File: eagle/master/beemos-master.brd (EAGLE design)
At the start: 99.1 x 73.7 mm, 47 parts, among them CON1 BAT, CON2 JACK_DC_BARREL, CON3 SPI, IC1 32U4, IC2 MCP73831T, IC3 MCP1703CB, IC4 DMP1045U, J1 RJ123.3, J10 RJ12STRAIGHT-I2C, J2 RJ123.3, J3 RJ123.3, J4 RJ123.3, J5 RJ123.3, J6 RJ123.3, J8 RJ123.3, J9 RJ12STRAIGHT-I2C, X1 8MHz, X2 MINI-USB

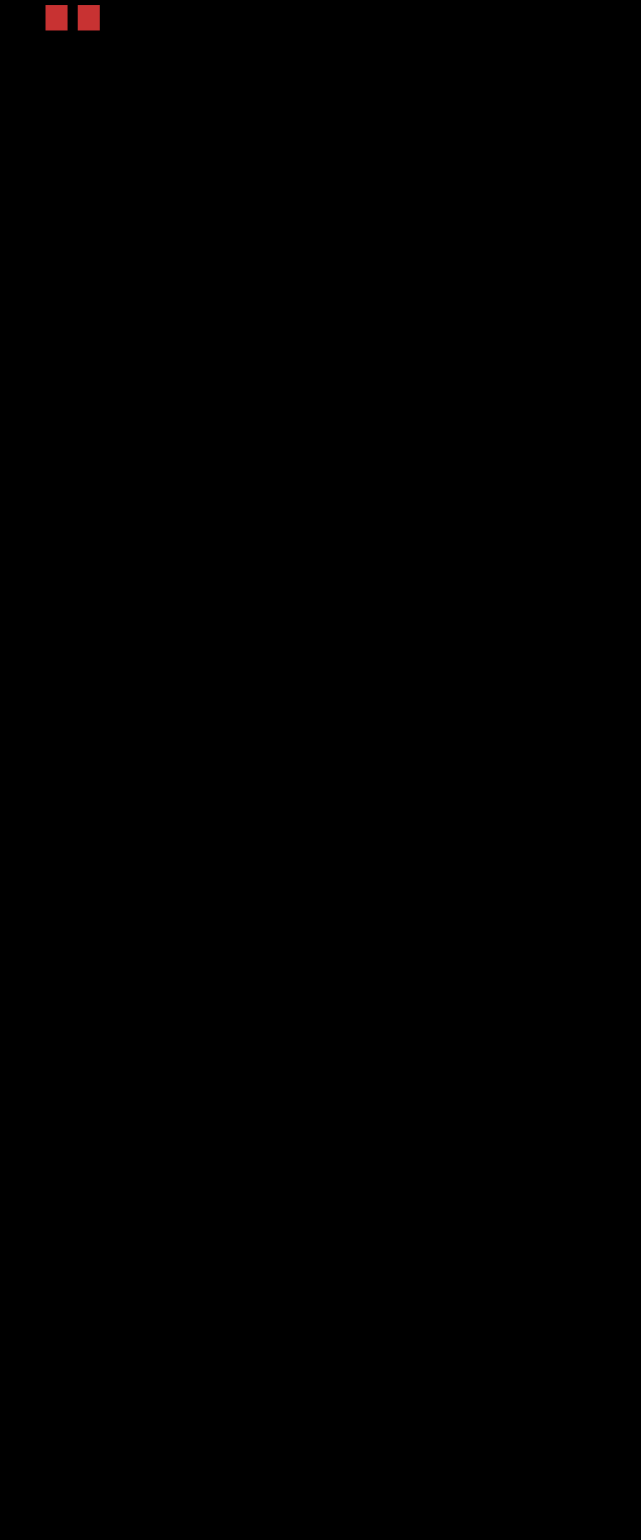
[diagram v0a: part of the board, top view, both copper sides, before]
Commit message: Added LoRa and OneWire to schematics
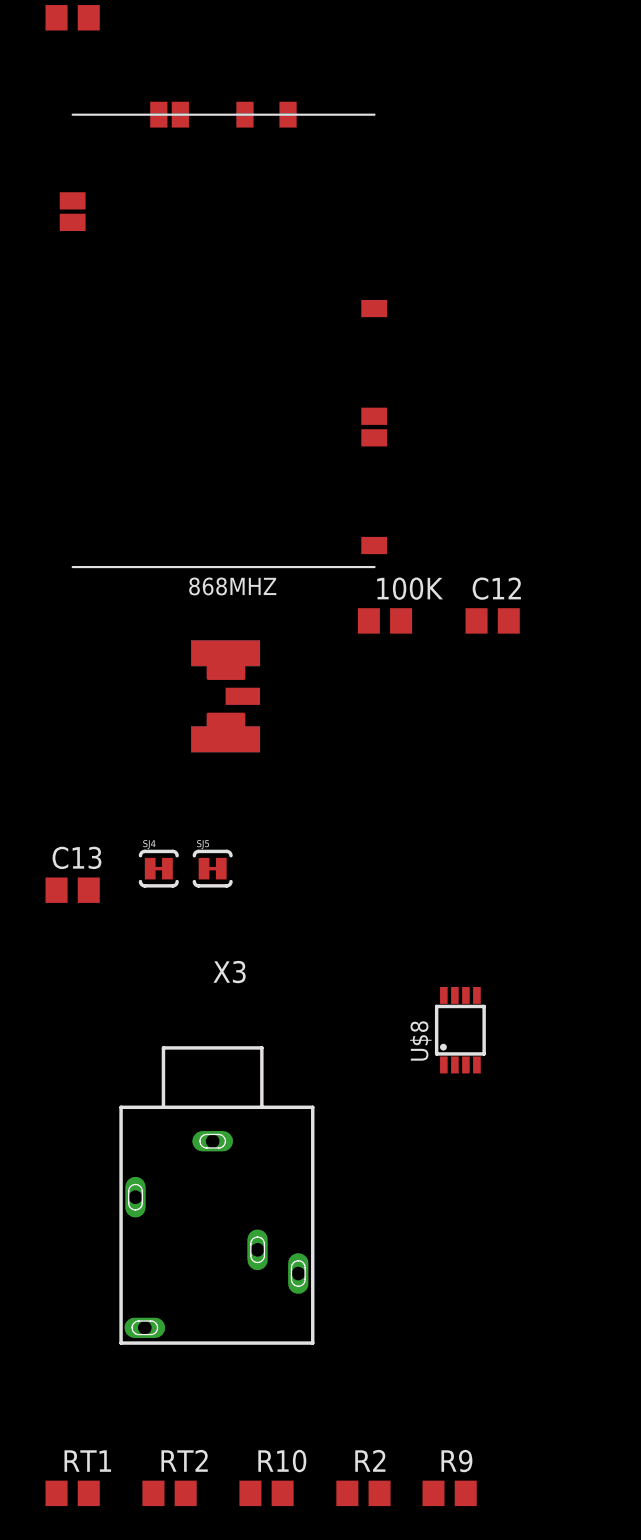
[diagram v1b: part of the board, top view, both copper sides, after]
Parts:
- added 100K: 100k, rcl:R0805
- added 868MHZ: (no value), sma_end_launch:SMA_EDGELAUNCH_UFL
- added C12, C13: 100n, rcl:C0805
- added R10, R9: 1K, rcl:R0805
- added R2: 100, rcl:R0805
- added RT1, RT2: 4.7k, resistor:R0805
- added SJ4, SJ5: (no value), SparkFun-Passives:PAD-JUMPER-2-NC_BY_TRACE_YES_SILK
- added U$7: RN2483_SIMPLE, Octanis1_bioreactorPort:RN2483_SIMPLE
- added U$8: DS18B20, lpatiny:MSOP8
- added X3: 1503_09, con-lumberg:1503_09
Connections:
- new net A7: R9.1
- new net ANGND: 868MHZ.GND@1, 868MHZ.GND@2, 868MHZ.GND@3, 868MHZ.GND@4, C12.2, C13.2, SJ4.2, SJ5.2, U$7.P$1, U$7.P$21, U$7.P$26, U$7.P$27, U$7.P$33
- new net ANT868: 868MHZ.P, U$7.P$23
- new net D12*: R10.1
- new net N$14: R2.1, RT1.1, X3.1
- new net N$21: R9.2, RT1.2, X3.2
- new net N$9: R10.2, RT2.2, U$8.1
- net 3.3V: now also 100K.1, C12.1, C13.1, R2.2, RT2.1, U$7.P$12, U$8.8
- net A2: now also 100K.2, U$7.P$32
- net GND: now also SJ4.1, SJ5.1, U$8.4, X3.3
- net RX: now also U$7.P$6
- net TX: now also U$7.P$7
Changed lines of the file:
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@@
 <?xml version="1.0" encoding="utf-8"?>
 <!DOCTYPE eagle SYSTEM "eagle.dtd">
-<eagle version="8.7.1">
+<eagle version="9.0.0">
 <drawing>
 <settings>
-<setting alwaysvectorfont="yes"/>
+<setting alwaysvectorfont="no"/>
 <setting keepoldvectorfont="yes"/>
 <setting verticaltext="up"/>
@@
 </variantdefs>
 <classes>
-<class number="0" name="default" width="0.4064" drill="0">
+<class number="0" name="default" width="0.2032" drill="0">
 <clearance class="0" value="0.25"/>
 </class>
-<class number="1" name="power" width="0.4064" drill="0.3048">
+<class number="1" name="power" width="0.2032" drill="0.3048">
 <clearance class="1" value="0.25"/>
 </class>
@@
 <element name="R6" library="rcl" package="R0805" value="4.7k" x="-11.43" y="-63.5"/>
 <element name="U$6" library="SIM800L" package="SIP" value="SIM800L" x="93.98" y="22.225" rot="MR0"/>
+<element name="C12" library="rcl" package="C0805" value="100n" x="13.335" y="-99.06"/>
+<element name="C13" library="rcl" package="C0805" value="100n" x="-11.43" y="-114.935"/>
+<element name="SJ4" library="SparkFun-Passives" package="PAD-JUMPER-2-NC_BY_TRACE_YES_SILK" value="" x="-6.35" y="-113.665"/>
+<element name="SJ5" library="SparkFun-Passives" package="PAD-JUMPER-2-NC_BY_TRACE_YES_SILK" value="" x="-3.175" y="-113.665"/>
+<element name="100K" library="rcl" package="R0805" value="100k" x="6.985" y="-99.06"/>
+<element name="868MHZ" library="sma_end_launch" package="SMA_EDGELAUNCH_UFL" value="" x="-4.445" y="-103.505"/>
+<element name="U$7" library="Octanis1_bioreactorPort" package="RN2483_SIMPLE" value="RN2483_SIMPLE" x="-2.54" y="-83.185"/>
+<element name="RT1" library="resistor" package="R0805" value="4.7k" x="-11.43" y="-150.495"/>
+<element name="RT2" library="resistor" package="R0805" value="4.7k" x="-5.715" y="-150.495"/>
+<element name="R9" library="rcl" package="R0805" value="1K" x="10.795" y="-150.495"/>
+<element name="R10" library="rcl" package="R0805" value="1K" x="0" y="-150.495"/>
+<element name="X3" library="con-lumberg" package="1503_09" value="1503_09" x="-3.175" y="-127.635">
+<attribute name="MF" value="" x="-25.4" y="-123.19" size="1.778" layer="27" display="off"/>
+<attribute name="MPN" value="" x="-25.4" y="-123.19" size="1.778" layer="27" display="off"/>
+<attribute name="OC_FARNELL" value="1243244" x="-25.4" y="-123.19" size="1.778" layer="27" display="off"/>
+<attribute name="OC_NEWARK" value="unknown" x="-25.4" y="-123.19" size="1.778" layer="27" display="off"/>
+</element>
+<element name="U$8" library="lpatiny" package="MSOP8" value="DS18B20" x="11.43" y="-123.19"/>
+<element name="R2" library="rcl" package="R0805" value="100" x="5.715" y="-150.495"/>
 </elements>
 <signals>
@@
 <via x="88.265" y="12.7" extent="1-16" drill="0.35"/>
 <wire x1="88.265" y1="12.7" x2="88.9" y2="12.7" width="0.4064" layer="16"/>
+<contactref element="SJ4" pad="1"/>
+<contactref element="SJ5" pad="1"/>
+<contactref element="U$8" pad="4"/>
+<contactref element="X3" pad="3"/>
 <wire x1="67.31" y1="67.945" x2="84.455" y2="67.58" width="0" layer="19" extent="1-1"/>
 <wire x1="66.23" y1="50.885" x2="67.31" y2="67.945" width="0" layer="19" extent="1-1"/>
@@
 <wire x1="-8.255" y1="-38.6334" x2="-9.525" y2="-38.6334" width="0" layer="19" extent="1-1"/>
 <wire x1="-6.985" y1="-38.6334" x2="-8.255" y2="-38.6334" width="0" layer="19" extent="1-1"/>
+<wire x1="-6.858" y1="-113.665" x2="-6.985" y2="-38.6334" width="0" layer="19" extent="1-1"/>
+<wire x1="-3.683" y1="-113.665" x2="-6.858" y2="-113.665" width="0" layer="19" extent="1-1"/>
+<wire x1="12.405" y1="-125.24" x2="-3.683" y2="-113.665" width="0" layer="19" extent="1-1"/>
+<wire x1="1.875" y1="-137.535" x2="12.405" y2="-125.24" width="0" layer="19" extent="1-1"/>
 </signal>
 <signal name="SCK">
@@
 <contactref element="IC1" pad="38"/>
 <contactref element="J3" pad="I/O"/>
+<contactref element="100K" pad="2"/>
+<contactref element="U$7" pad="P$32"/>
 <wire x1="56.43" y1="45.885" x2="51.435" y2="70.485" width="0" layer="19" extent="1-1"/>
+<wire x1="-11.43" y1="-75.565" x2="56.43" y2="45.885" width="0" layer="19" extent="1-1"/>
+<wire x1="7.935" y1="-99.06" x2="-11.43" y2="-75.565" width="0" layer="19" extent="1-1"/>
 </signal>
 <signal name="A3">
@@
 <contactref element="IC1" pad="21"/>
 <contactref element="U$6" pad="5"/>
+<contactref element="U$7" pad="P$7"/>
 <wire x1="55.88" y1="31.305" x2="68.03" y2="48.285" width="0" layer="19" extent="1-1"/>
+<wire x1="6.35" y1="-86.995" x2="55.88" y2="31.305" width="0" layer="19" extent="1-1"/>
 </signal>
 <signal name="RX">
 <contactref element="IC1" pad="20"/>
 <contactref element="U$6" pad="4"/>
+<contactref element="U$7" pad="P$6"/>
 <wire x1="55.88" y1="33.845" x2="68.03" y2="47.485" width="0" layer="19" extent="1-1"/>
+<wire x1="6.35" y1="-88.265" x2="55.88" y2="33.845" width="0" layer="19" extent="1-1"/>
 </signal>
 <signal name="D7">
@@
 <wire x1="74.93" y1="20.955" x2="74.93" y2="3.175" width="0.508" layer="1"/>
 <wire x1="74.93" y1="3.175" x2="69.215" y2="3.175" width="0.508" layer="1"/>
-<wire x1="66.04" y1="70.485" x2="83.185" y2="70.12" width="0" layer="19" extent="1-1"/>
+<contactref element="C12" pad="1"/>
+<contactref element="100K" pad="1"/>
+<contactref element="C13" pad="1"/>
+<contactref element="U$7" pad="P$12"/>
+<contactref element="RT2" pad="1"/>
+<contactref element="U$8" pad="8"/>
+<contactref element="R2" pad="2"/>
+<wire x1="6.665" y1="-150.495" x2="-6.665" y2="-150.495" width="0" layer="19" extent="1-1"/>
+<wire x1="10.455" y1="-121.14" x2="6.665" y2="-150.495" width="0" layer="19" extent="1-1"/>
+<wire x1="12.385" y1="-99.06" x2="10.455" y2="-121.14" width="0" layer="19" extent="1-1"/>
+<wire x1="6.035" y1="-99.06" x2="12.385" y2="-99.06" width="0" layer="19" extent="1-1"/>
+<wire x1="6.35" y1="-80.645" x2="6.035" y2="-99.06" width="0" layer="19" extent="1-1"/>
+<wire x1="-12.38" y1="-114.935" x2="10.455" y2="-121.14" width="0" layer="19" extent="1-1"/>
+<wire x1="14.22976875" y1="19.413" x2="6.35" y2="-80.645" width="0" layer="19" extent="1-1"/>
+<wire x1="66.04" y1="70.485" x2="65.43" y2="50.885" width="0" layer="19" extent="1-1"/>
+<wire x1="83.185" y1="70.12" x2="66.04" y2="70.485" width="0" layer="19" extent="1-1"/>
 <wire x1="48.895" y1="70.485" x2="66.04" y2="70.485" width="0" layer="19" extent="1-1"/>
 <wire x1="30.48" y1="70.485" x2="48.895" y2="70.485" width="0" layer="19" extent="1-1"/>
 <wire x1="13.335" y1="70.485" x2="30.48" y2="70.485" width="0" layer="19" extent="1-1"/>
-<wire x1="65.43" y1="50.885" x2="66.04" y2="70.485" width="0" layer="19" extent="1-1"/>
 </signal>
 <signal name="D14" class="1">
@@
 <wire x1="-10.795" y1="-32.4866" x2="-10.48" y2="-57.15" width="0" layer="19" extent="1-1"/>
 </signal>
+<signal name="ANT868">
+<contactref element="868MHZ" pad="P"/>
+<contactref element="U$7" pad="P$23"/>
+<wire x1="-1.27" y1="-69.215" x2="-1.397" y2="-103.505" width="0" layer="19" extent="1-1"/>
+</signal>
+<signal name="ANGND">
+<contactref element="U$7" pad="P$1"/>
+<contactref element="U$7" pad="P$33"/>
+<contactref element="SJ4" pad="2"/>
+<contactref element="SJ5" pad="2"/>
+<contactref element="868MHZ" pad="GND@4"/>
+<contactref element="868MHZ" pad="GND@3"/>
+<contactref element="868MHZ" pad="GND@2"/>
+<contactref element="868MHZ" pad="GND@1"/>
+<contactref element="U$7" pad="P$21"/>
+<contactref element="U$7" pad="P$26"/>
+<contactref element="U$7" pad="P$27"/>
+<contactref element="C12" pad="2"/>
+<contactref element="C13" pad="2"/>
+<wire x1="-5.842" y1="-113.665" x2="-10.48" y2="-114.935" width="0" layer="19" extent="1-1"/>
+<wire x1="-2.667" y1="-113.665" x2="-5.842" y2="-113.665" width="0" layer="19" extent="1-1"/>
+<wire x1="-2.413" y1="-106.045" x2="-2.667" y2="-113.665" width="0" layer="19" extent="1-16"/>
+<wire x1="-2.413" y1="-106.045" x2="-2.413" y2="-106.045" width="0" layer="19" extent="1-16"/>
+<wire x1="-2.413" y1="-100.965" x2="-2.413" y2="-106.045" width="0" layer="19" extent="16-16"/>
+<wire x1="-2.413" y1="-100.965" x2="-2.413" y2="-100.965" width="0" layer="19" extent="1-16"/>
+<wire x1="6.35" y1="-94.615" x2="-2.413" y2="-100.965" width="0" layer="19" extent="1-16"/>
+<wire x1="14.285" y1="-99.06" x2="6.35" y2="-94.615" width="0" layer="19" extent="1-1"/>
+<wire x1="1.27" y1="-69.215" x2="6.35" y2="-94.615" width="0" layer="19" extent="1-1"/>
+<wire x1="-5.08" y1="-69.215" x2="1.27" y2="-69.215" width="0" layer="19" extent="1-1"/>
+<wire x1="-6.35" y1="-69.215" x2="-5.08" y2="-69.215" width="0" layer="19" extent="1-1"/>
+<wire x1="-11.43" y1="-74.295" x2="-6.35" y2="-69.215" width="0" layer="19" extent="1-1"/>
+</signal>
+<signal name="D12*">
+<contactref element="R10" pad="1"/>
+</signal>
+<signal name="N$9" class="1">
+<contactref element="RT2" pad="2"/>
+<contactref element="R10" pad="2"/>
+<contactref element="U$8" pad="1"/>
+<wire x1="0.95" y1="-150.495" x2="-4.765" y2="-150.495" width="0" layer="19" extent="1-1"/>
+<wire x1="10.455" y1="-125.24" x2="0.95" y2="-150.495" width="0" layer="19" extent="1-1"/>
+</signal>
+<signal name="N$21" class="1">
+<contactref element="RT1" pad="2"/>
+<contactref element="R9" pad="2"/>
+<contactref element="X3" pad="2"/>
+<wire x1="-7.725" y1="-133.035" x2="-10.48" y2="-150.495" width="0" layer="19" extent="1-1"/>
+<wire x1="11.745" y1="-150.495" x2="-10.48" y2="-150.495" width="0" layer="19" extent="1-1"/>
+</signal>
+<signal name="A7">
+<contactref element="R9" pad="1"/>
+</signal>
+<signal name="N$14" class="1">
+<contactref element="RT1" pad="1"/>
+<contactref element="X3" pad="1"/>
+<contactref element="R2" pad="1"/>
+<wire x1="4.765" y1="-150.495" x2="-12.38" y2="-150.495" width="0" layer="19" extent="1-1"/>
+<wire x1="-3.175" y1="-129.735" x2="4.765" y2="-150.495" width="0" layer="19" extent="1-1"/>
+</signal>
 </signals>

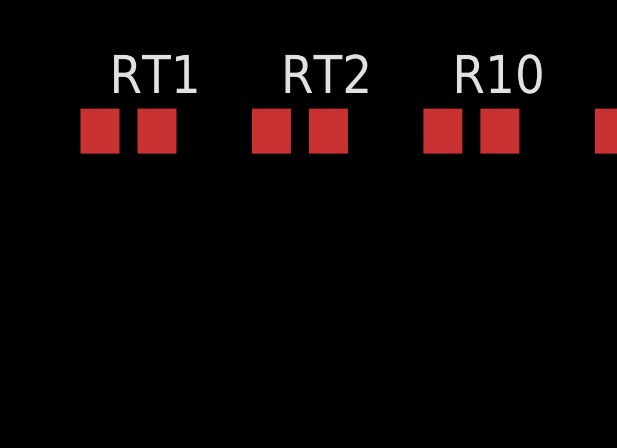
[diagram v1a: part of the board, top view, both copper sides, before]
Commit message: added bee counter PCB soldering doc v1.0
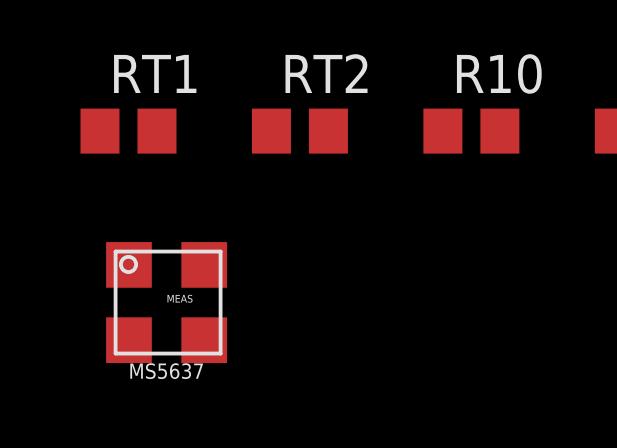
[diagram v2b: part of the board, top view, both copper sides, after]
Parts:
- added IC5: MS5637WIDE, MS5637:MS5637WIDE
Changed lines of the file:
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@@
 <element name="U$8" library="lpatiny" package="MSOP8" value="DS18B20" x="11.43" y="-123.19"/>
 <element name="R2" library="rcl" package="R0805" value="100" x="5.715" y="-150.495"/>
+<element name="IC5" library="MS5637" package="MS5637WIDE" value="MS5637WIDE" x="-10.16" y="-156.21"/>
 </elements>
 <signals>
